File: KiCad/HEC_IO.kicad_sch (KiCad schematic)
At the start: 22 parts, among them J2 Conn_02x12_Odd_Even, SW1 SW_DIP_x04, U12 74LS04, U17 74LS20, U22 74LS02, U30 74LS74, U31 74LS32, U32 LM79M05_TO220, U33 74LS20, U34 74LS393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

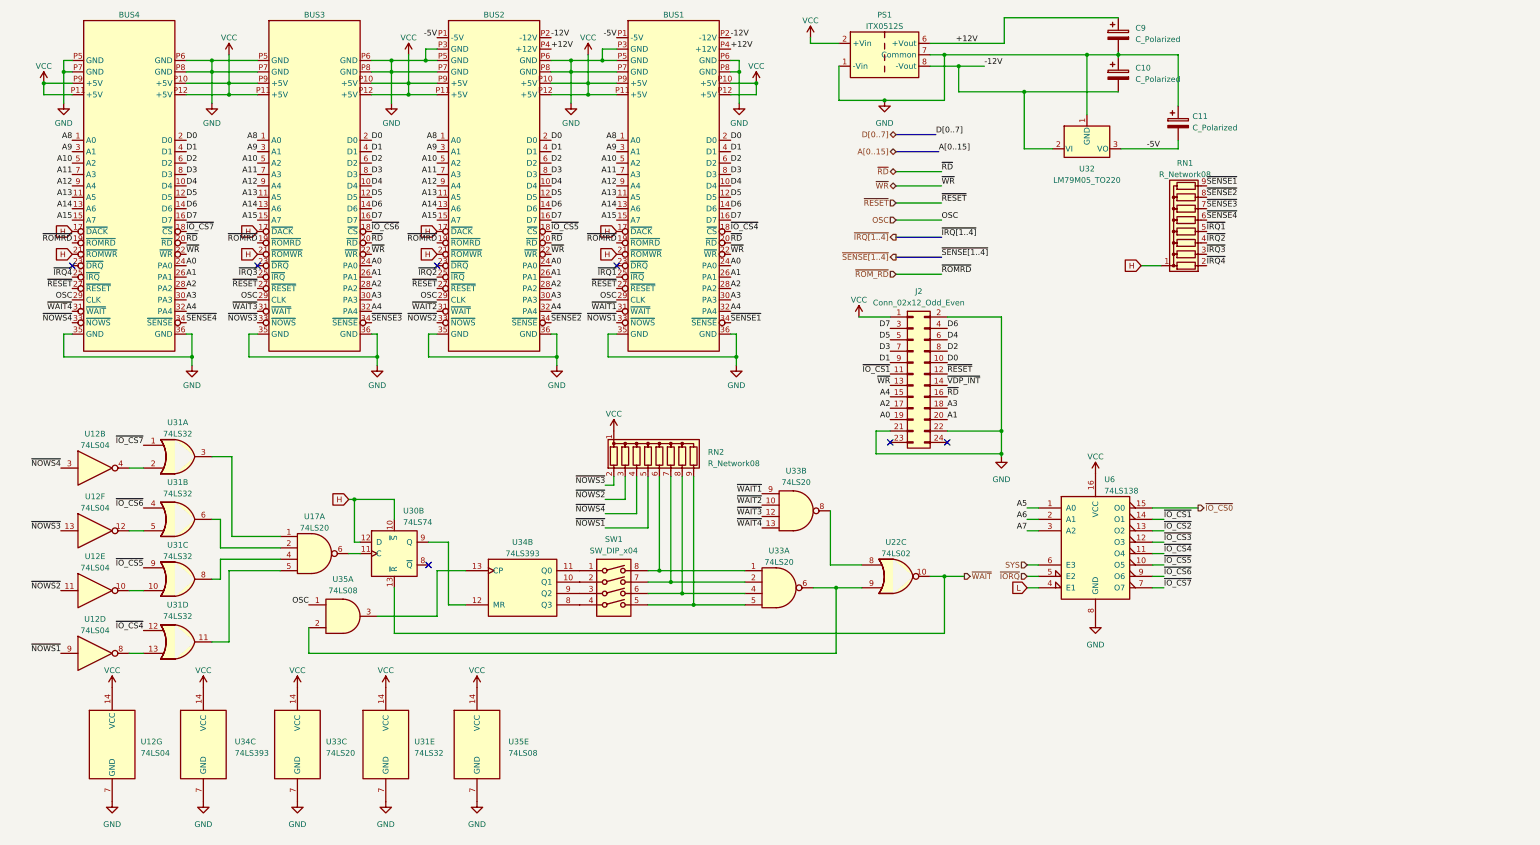
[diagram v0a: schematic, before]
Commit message: Cleanup schematic
Cleanup the schematic for easier reading, reduce ERC errors.
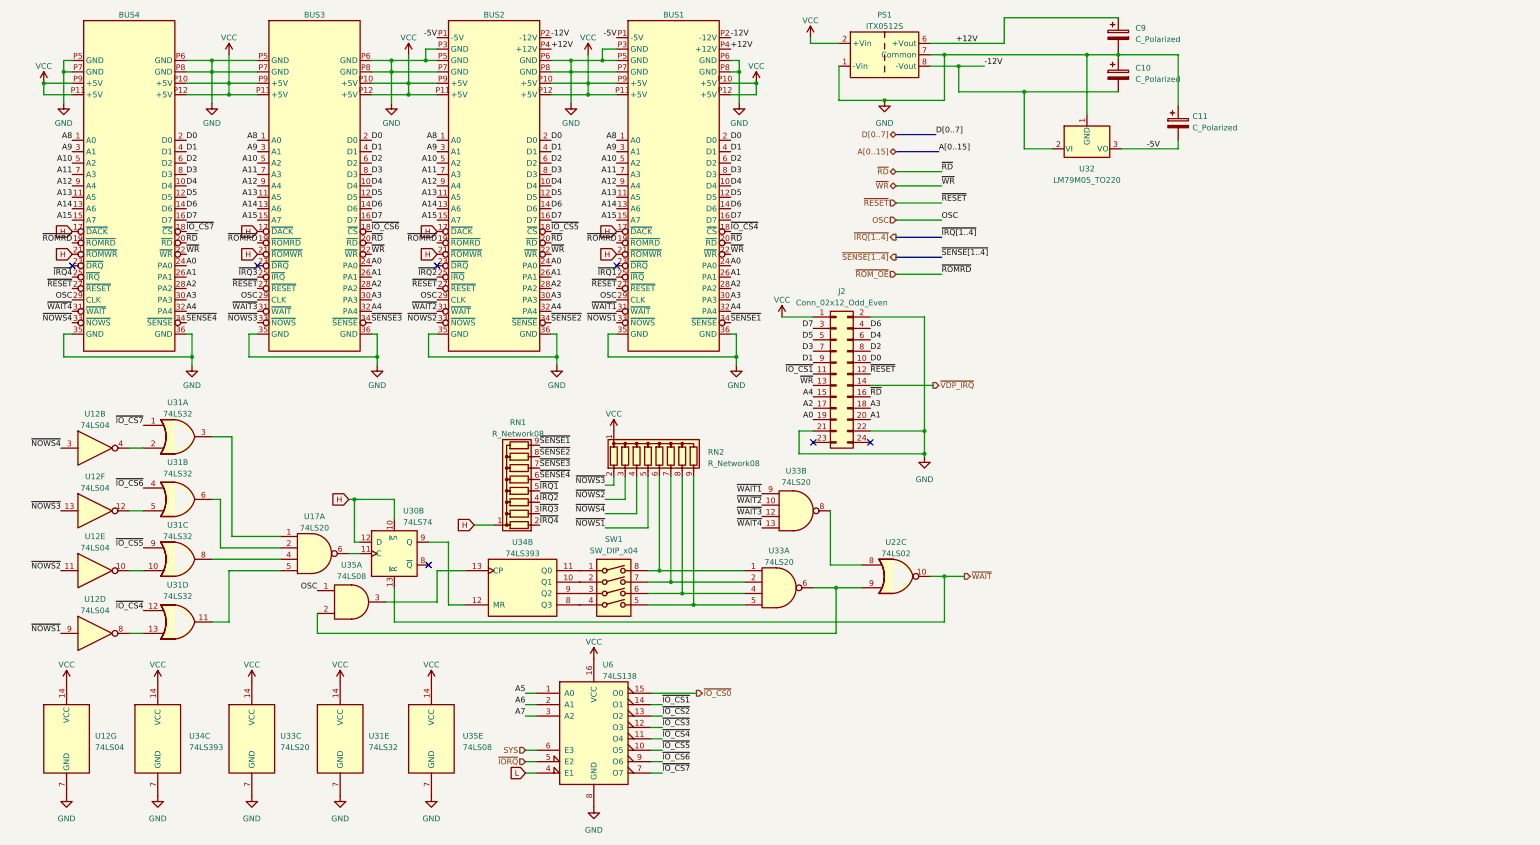
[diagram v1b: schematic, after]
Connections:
- net ~{ROM_RD} renamed ~{ROM_OE}
- net ~{VDP_INT} renamed ~{VDP_IRQ}
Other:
- moved on the sheet: J2, RN1, U12B, U12D, U12E, U12F, U12G, U31A, U31B, U31C, U31D, U31E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

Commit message: Add keyboard circuit
Added symbol for HT6542B keyboard controller. Added keyboard and mouse support to IO circuit. Reduced ERC error to 0.
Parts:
- added J4, J5: Mini-DIN-6, symbol Connector:Mini-DIN-6
- added RN5: R_Network07, Resistor_THT:R_Array_SIP8, symbol Device:R_Network07
- added U42: ~, symbol New_Library:HT6542B
- added U43: 74LS06, symbol 74xx:74LS06
- added Y1: Crystal, symbol Device:Crystal
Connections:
- net A0: now also U42.9 (A0)
- net D0: now also U42.12 (D0)
- net D1: now also U42.13 (D1)
- net D2: now also U42.14 (D2)
- net D3: now also U42.15 (D3)
- net D4: now also U42.16 (D4)
- net D5: now also U42.17 (D5)
- net D6: now also U42.18 (D6)
- net D7: now also U42.19 (D7)
- net GND: now also J4.3, J5.3, U42.20 (GND), U43.7 (GND)
- net VCC: now also J4.4, J5.4, RN5.1 (common), U42.26 (TEST), U42.40 (VCC), U43.14 (VCC)
- net ~{IO_CS2}: now also U42.6 (~{CS})
- net ~{RD}: now also U42.8 (~{RD})
- net ~{RESET}: now also U42.4 (~{RESET})
- net ~{WR}: now also U42.10 (~{WR})
- new net: U42.2 (OSCI), Y1.1
- new net: U42.3 (OSCO), Y1.2
- new net: U42.23 (P22/MSDO), U43.1
- new net: J4.1, RN5.3 (R2), U42.28 (P11/MSDI), U43.2
- new net: U42.24 (P23/MSCO), U43.3
- new net: J4.5, RN5.4 (R3), U42.39 (KBDI/MSCI), U43.4
- new net: U42.38 (KBDO), U43.5
- new net: J5.1, RN5.5 (R4), U42.27 (P10/KBDI), U43.6
- new net: J5.5, RN5.6 (R5), U42.1 (KBCI), U43.8
- new net: U42.37 (KBCO), U43.9
- new net: U42.35 (KB_OBFO), U43.11
- new net: U42.36 (MS_OBFO), U43.13
- new net: RN5.2 (R1), U42.34 (~{KBD_INH})
- new net ~{KB_IRQ}: RN5.8 (R7), U43.10
- new net ~{MS_IRQ}: RN5.7 (R6), U43.12
- no-connect marks 7 -> 19

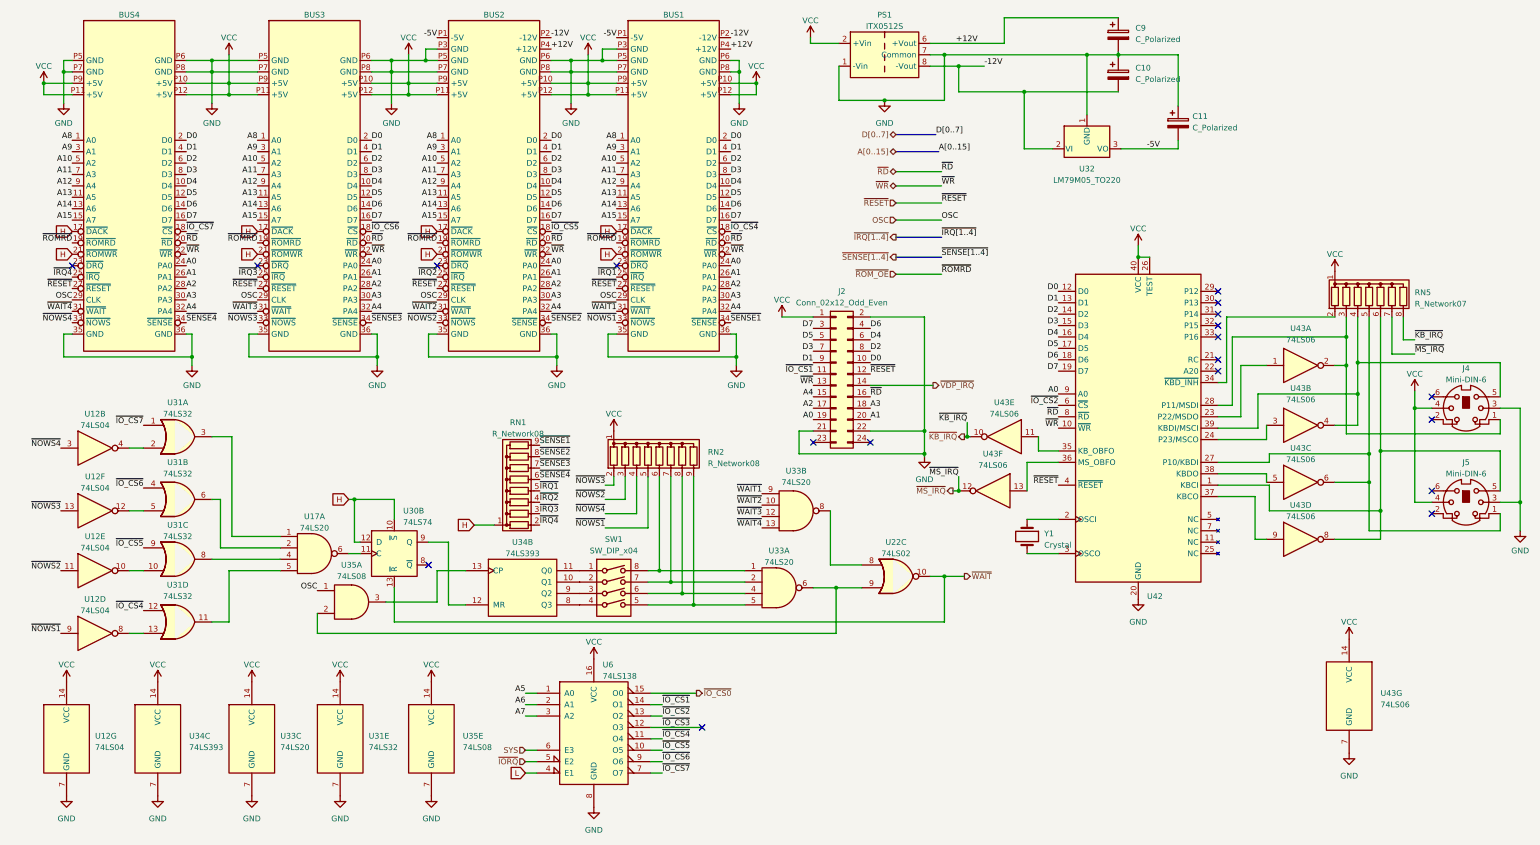
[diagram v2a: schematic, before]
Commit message: Split peripherals into separate schematic
Split graphics/sound/storage (VERA) board connector and keyboard/mouse controller into a separate schematic file. Add joystick/controller port. This commit is seriously delayed by the controller port design, and it is still subject to change.
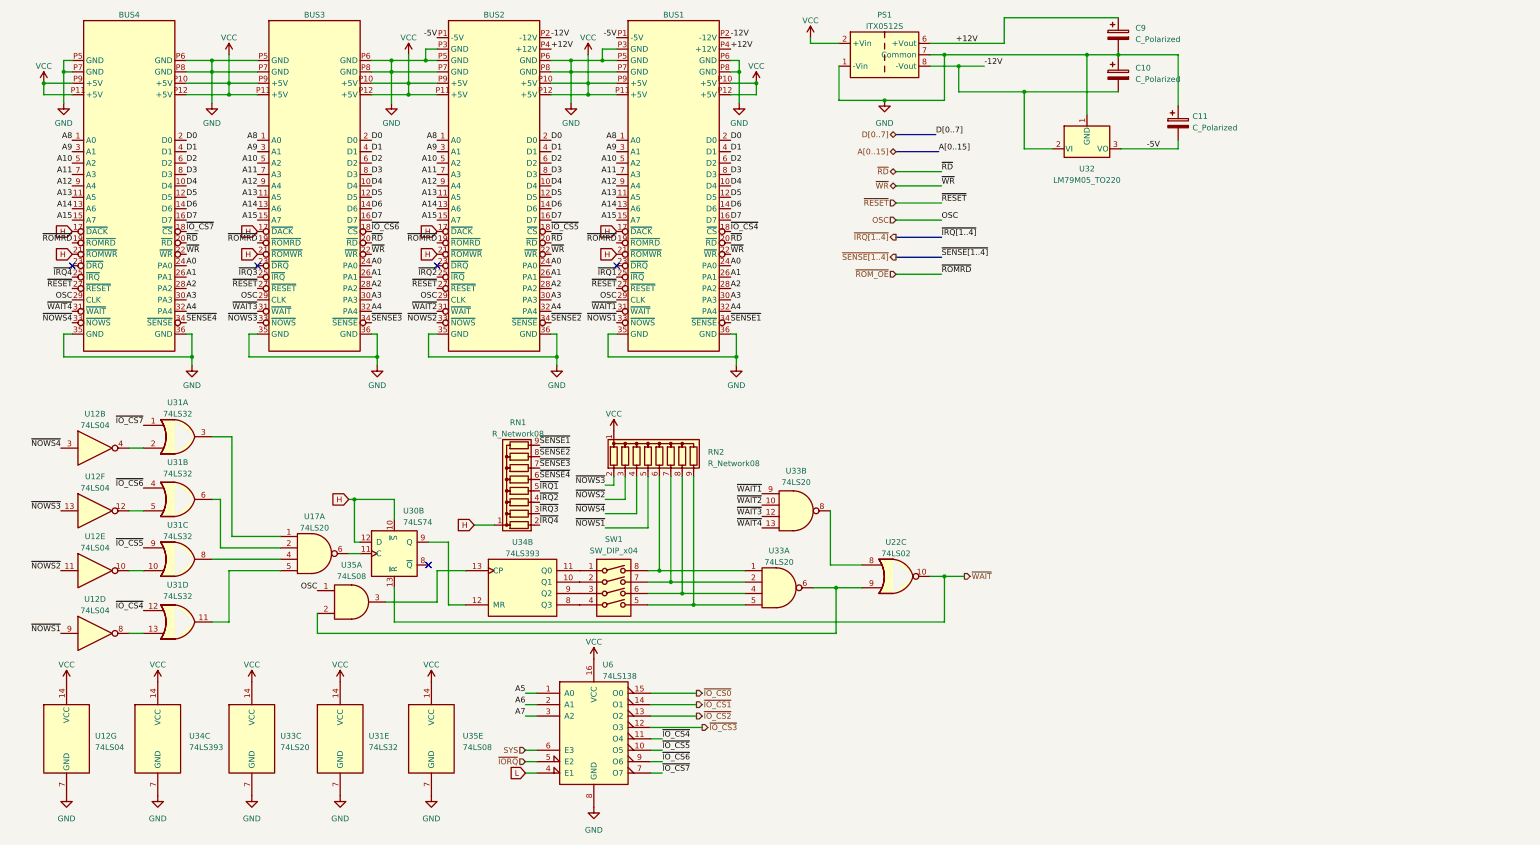
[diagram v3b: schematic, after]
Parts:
- removed J2: Conn_02x12_Odd_Even, Connector_PinHeader_2.54mm:PinHeader_2x12_P2.54mm_Vertical, symbol Connector_Generic:Conn_02x12_Odd_Even
- removed J4, J5: Mini-DIN-6, symbol Connector:Mini-DIN-6
- removed RN5: R_Network07, Resistor_THT:R_Array_SIP8, symbol Device:R_Network07
- removed U42: ~, symbol New_Library:HT6542B
- removed U43: 74LS06, symbol 74xx:74LS06
- removed Y1: Crystal, symbol Device:Crystal
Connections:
- no-connect marks 19 -> 5

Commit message: Removed DMA from bus
Bus-mastering DMA has been removed from the expansion bus design due to complexity and bandwidth issue with external bus expansion circuit. The pins are replaced with audio output from on-bard sound system. Minor changes to pin names.
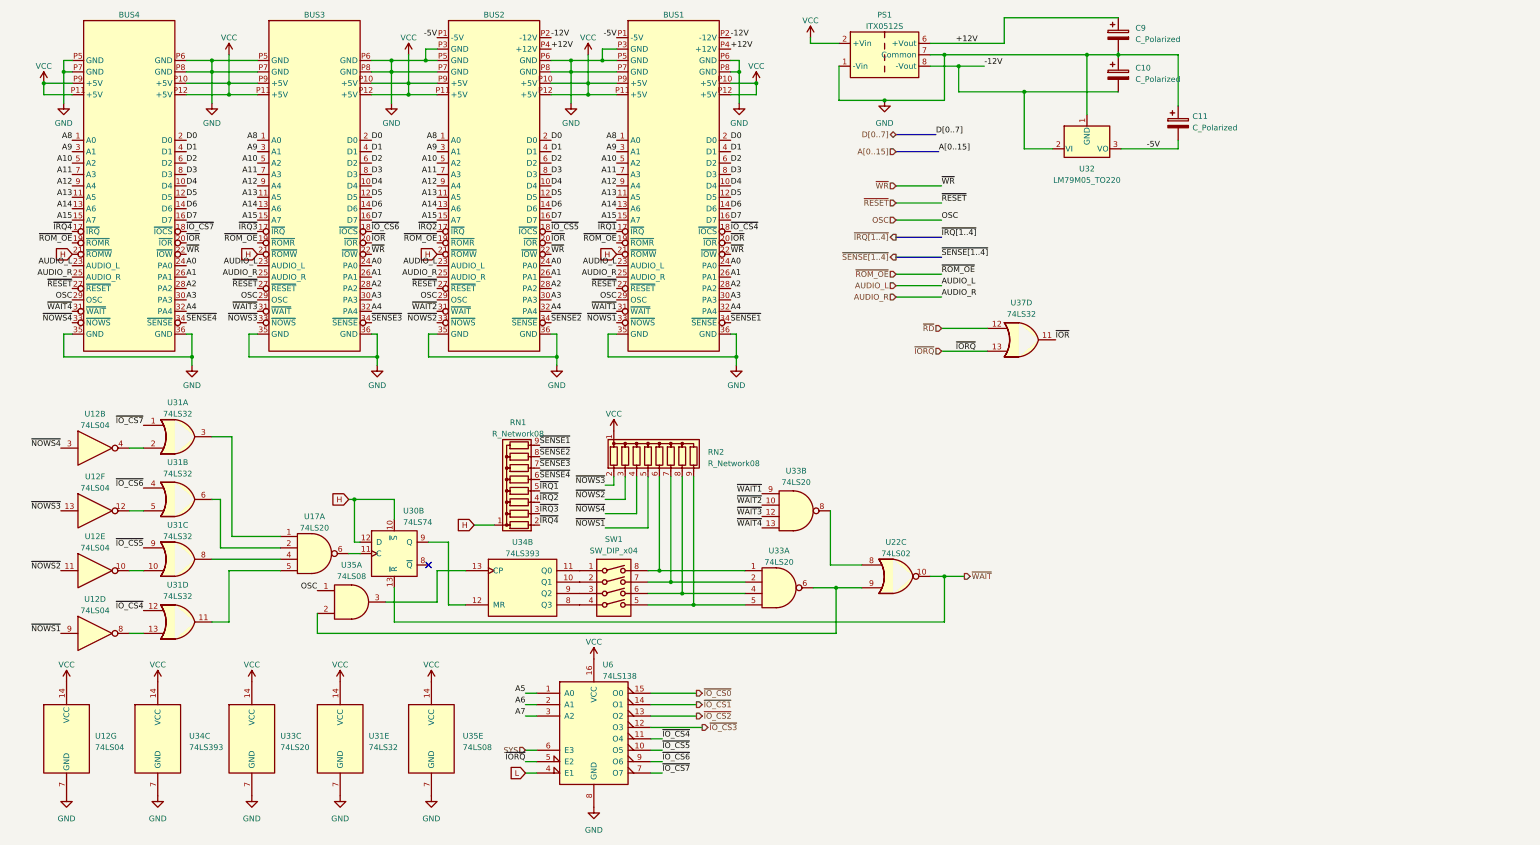
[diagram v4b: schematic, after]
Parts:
- added U37: 74LS32, Package_DIP:DIP-14_W7.62mm_Socket, symbol 74xx:74LS32
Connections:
- net H: no longer BUS1.17 (~{DACK}), BUS2.17 (~{DACK}), BUS3.17 (~{DACK}), BUS4.17 (~{DACK})
- net ~{IORQ}: now also U37.13
- net ~{IRQ1}: now also BUS1.17 (~{IRQ}); no longer BUS1.25 (~{IRQ})
- net ~{IRQ2}: now also BUS2.17 (~{IRQ}); no longer BUS2.25 (~{IRQ})
- net ~{IRQ3}: now also BUS3.17 (~{IRQ}); no longer BUS3.25 (~{IRQ})
- net ~{IRQ4}: now also BUS4.17 (~{IRQ}); no longer BUS4.25 (~{IRQ})
- net ~{RD}: now also U37.12; no longer BUS1.20 (~{RD}), BUS2.20 (~{RD}), BUS3.20 (~{RD}), BUS4.20 (~{RD})
- net AUDIO_L: now reaches BUS2.23 (AUDIO_L)
- net AUDIO_L: now also BUS1.23 (AUDIO_L), BUS3.23 (AUDIO_L), BUS4.23 (AUDIO_L)
- new net AUDIO_R: BUS1.25 (AUDIO_R), BUS2.25 (AUDIO_R), BUS3.25 (AUDIO_R), BUS4.25 (AUDIO_R)
- new net ~{IOR}: BUS1.20 (~{IOR}), BUS2.20 (~{IOR}), BUS3.20 (~{IOR}), BUS4.20 (~{IOR}), U37.11
- no-connect marks 5 -> 1

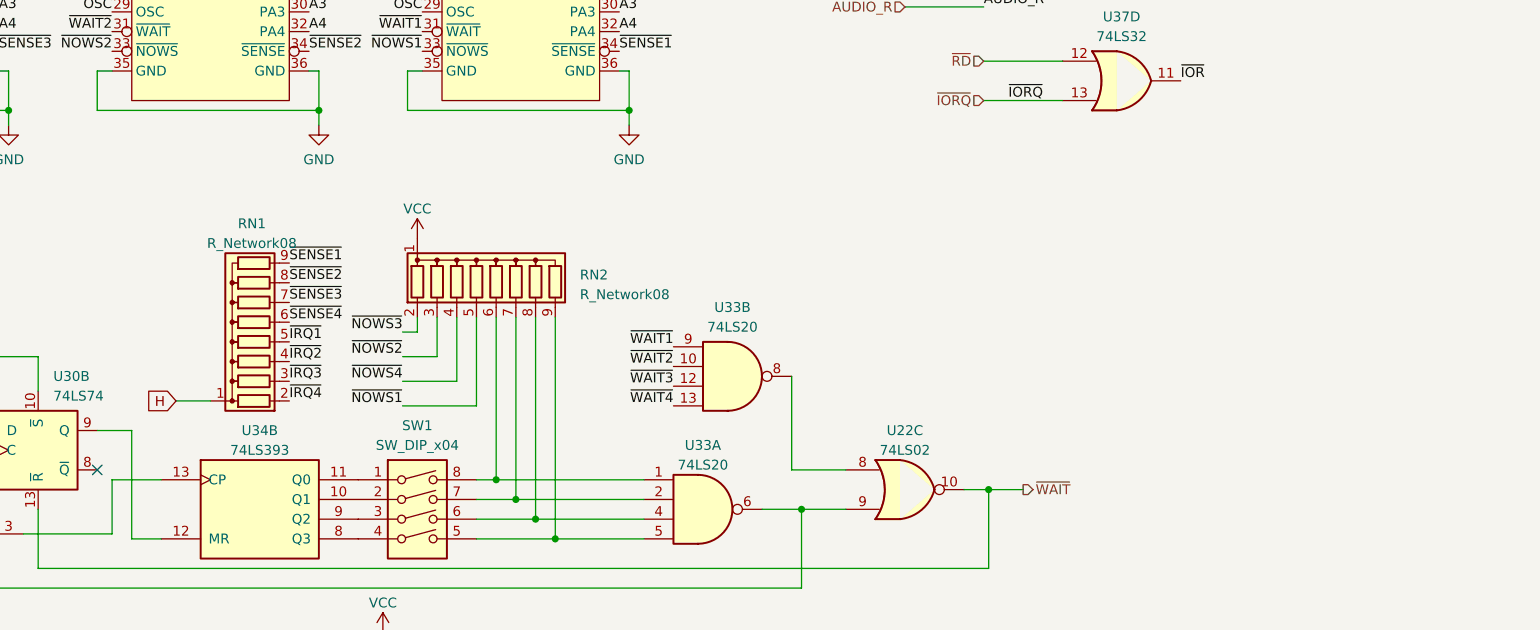
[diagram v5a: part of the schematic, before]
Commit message: Preliminary layout
Very early stage layout prototype, very subject to change.
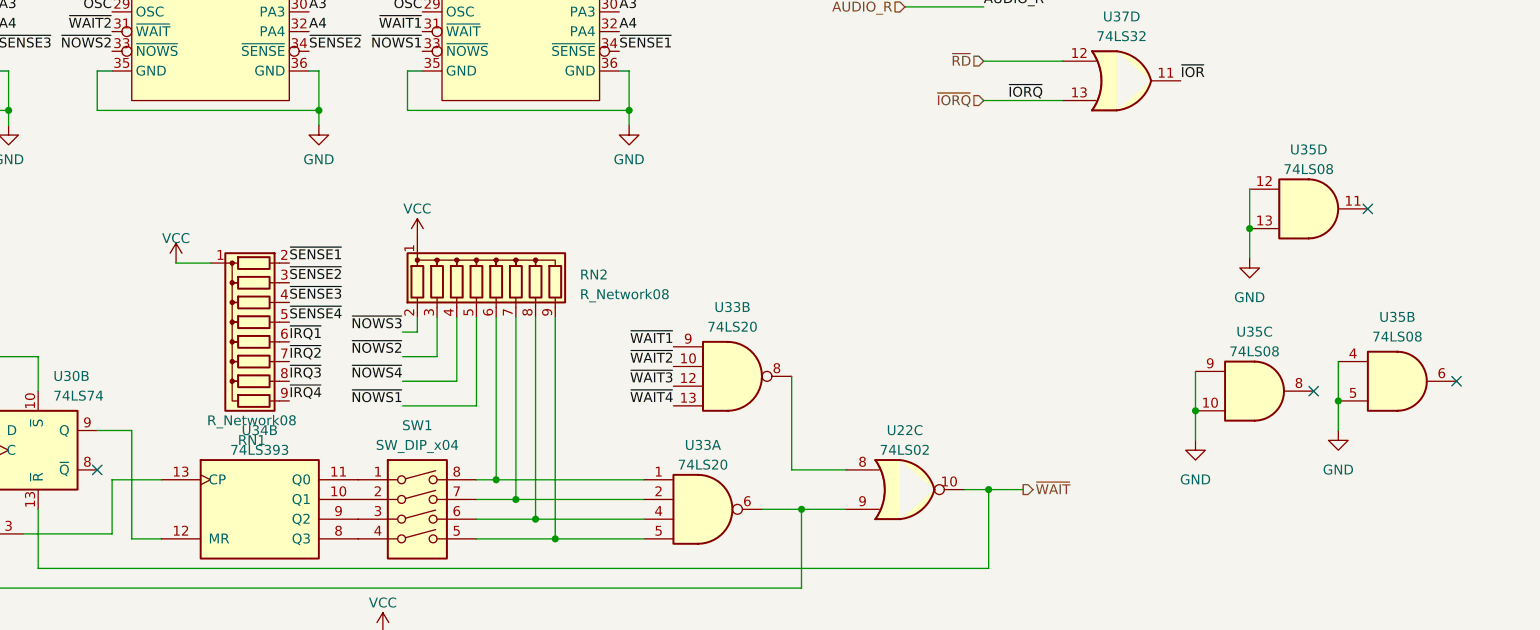
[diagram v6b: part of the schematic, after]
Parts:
- added unit 3 of U35
- added unit 4 of U35
- added unit 2 of U35
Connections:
- net GND: now also U35.10, U35.12, U35.13, U35.4, U35.5, U35.9
- net H: no longer RN1.1 (common)
- net VCC: now also RN1.1 (common)
- net ~{IRQ1}: now also RN1.6 (R5); no longer RN1.5 (R4)
- net ~{IRQ2}: now also RN1.7 (R6); no longer RN1.4 (R3)
- net ~{IRQ3}: now also RN1.8 (R7); no longer RN1.3 (R2)
- net ~{IRQ4}: now also RN1.9 (R8); no longer RN1.2 (R1)
- net ~{SENSE1}: now also RN1.2 (R1); no longer RN1.9 (R8)
- net ~{SENSE2}: now also RN1.3 (R2); no longer RN1.8 (R7)
- net ~{SENSE3}: now also RN1.4 (R3); no longer RN1.7 (R6)
- net ~{SENSE4}: now also RN1.5 (R4); no longer RN1.6 (R5)
- no-connect marks 1 -> 4
